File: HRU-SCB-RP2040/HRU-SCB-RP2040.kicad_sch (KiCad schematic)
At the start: 7 parts, among them J26 Pico_Socket_A, J27 Pico_Socket_B

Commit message: update: circuit design of HRU-SCB-RP2040
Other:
- moved on the sheet: A1
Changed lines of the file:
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@@
 (kicad_sch
-	(version 20231120)
+	(version 20250114)
 	(generator "eeschema")
-	(generator_version "8.0")
+	(generator_version "9.0")
 	(paper "A4")
 	(junction
@@
 	(label "SERVO.SERIAL1.TX"
 		(at 132.08 40.64 0)
-		(fields_autoplaced yes)
 		(effects
 			(font
@@
 	(label "I2C0.SCL"
 		(at 215.9 27.94 0)
-		(fields_autoplaced yes)
 		(effects
 			(font
@@
 	(label "SERVO.SERIAL1.TX"
 		(at 33.02 63.5 0)
-		(fields_autoplaced yes)
 		(effects
 			(font
@@
 	(label "SERVO.SERIAL0.RX"
 		(at 132.08 27.94 0)
-		(fields_autoplaced yes)
 		(effects
 			(font
@@
 	(label "SERVO.SERIAL1.DE"
 		(at 33.02 50.8 0)
-		(fields_autoplaced yes)
 		(effects
 			(font
@@
 	(label "SERVO.SERIAL1.DE"
 		(at 132.08 43.18 0)
-		(fields_autoplaced yes)
 		(effects
 			(font
@@
 	(label "SERVO.SERIAL0.DE"
 		(at 132.08 33.02 0)
-		(fields_autoplaced yes)
 		(effects
 			(font
@@
 	(label "SERVO.SERIAL0.RX"
 		(at 33.02 45.72 0)
-		(fields_autoplaced yes)
 		(effects
 			(font
@@
 	(label "SERVO.SERIAL1.RX"
 		(at 33.02 66.04 0)
-		(fields_autoplaced yes)
 		(effects
 			(font
@@
 	(label "I2C0.SDA"
 		(at 215.9 30.48 0)
-		(fields_autoplaced yes)
 		(effects
 			(font
@@
 	(label "SERVO.SERIAL1.RX"
 		(at 132.08 38.1 0)
-		(fields_autoplaced yes)
 		(effects
 			(font
@@
 	(label "SERVO.SERIAL0.TX"
 		(at 132.08 30.48 0)
-		(fields_autoplaced yes)
 		(effects
 			(font
@@
 	(label "SERVO.SERIAL0.DE"
 		(at 33.02 48.26 0)
-		(fields_autoplaced yes)
 		(effects
 			(font
@@
 	(label "I2C0.SDA"
 		(at 33.02 53.34 0)
-		(fields_autoplaced yes)
 		(effects
 			(font
@@
 	(label "SERVO.SERIAL0.TX"
 		(at 33.02 43.18 0)
-		(fields_autoplaced yes)
 		(effects
 			(font
@@
 	(label "I2C0.SCL"
 		(at 33.02 55.88 0)
-		(fields_autoplaced yes)
 		(effects
 			(font
@@
 	(symbol
 		(lib_id "MCU_Module_RaspberryPi_Pico:RaspberryPi_Pico_W_MultiPart-Module")
-		(at 76.2 66.04 90)
+		(at 76.2 66.04 0)
 		(unit 1)
 		(exclude_from_sim no)
@@
 		(fields_autoplaced yes)
 		(property "Reference" "A1"
-			(at 35.56 58.42 0)
+			(at 83.82 25.4 0)
 			(do_not_autoplace yes)
 			(effects
@@
 		)
 		(property "Value" "RaspberryPi_Pico_W"
-			(at 38.1 58.42 0)
+			(at 83.82 27.94 0)
 			(do_not_autoplace yes)
 			(effects
@@
 		)
 		(property "Footprint" "Module_RaspberryPi_Pico:RaspberryPi_Pico_W_Virtual"
-			(at 125.73 66.04 0)
+			(at 76.2 115.57 0)
 			(effects
 				(font
@@
 		)
 		(property "Datasheet" "https://datasheets.raspberrypi.com/picow/pico-w-datasheet.pdf"
-			(at 128.27 66.04 0)
+			(at 76.2 118.11 0)
 			(effects
 				(font
@@
 		)
 		(property "Description" "Versatile and inexpensive wireless microcontroller module (virtual representation) powered by RP2040 dual-core Arm Cortex-M0+ processor up to 133 MHz, 264kB SRAM, 2MB QSPI flash, Infineon CYW43439 2.4GHz 802.11n wireless LAN"
-			(at 130.81 66.04 0)
+			(at 76.2 120.65 0)
 			(effects
 				(font
@@
 		(at 152.4 25.4)
 		(size 38.1 20.32)
+		(exclude_from_sim no)
+		(in_bom yes)
+		(on_board yes)
+		(dnp no)
 		(fields_autoplaced yes)
 		(stroke
@@
 		(at 152.4 63.5)
 		(size 38.1 25.4)
+		(exclude_from_sim no)
+		(in_bom yes)
+		(on_board yes)
+		(dnp no)
 		(fields_autoplaced yes)
 		(stroke
@@
 		(at 228.6 25.4)
 		(size 38.1 38.1)
+		(exclude_from_sim no)
+		(in_bom yes)
+		(on_board yes)
+		(dnp no)
 		(fields_autoplaced yes)
 		(stroke
@@
 		)
 	)
+	(embedded_fonts no)
 )

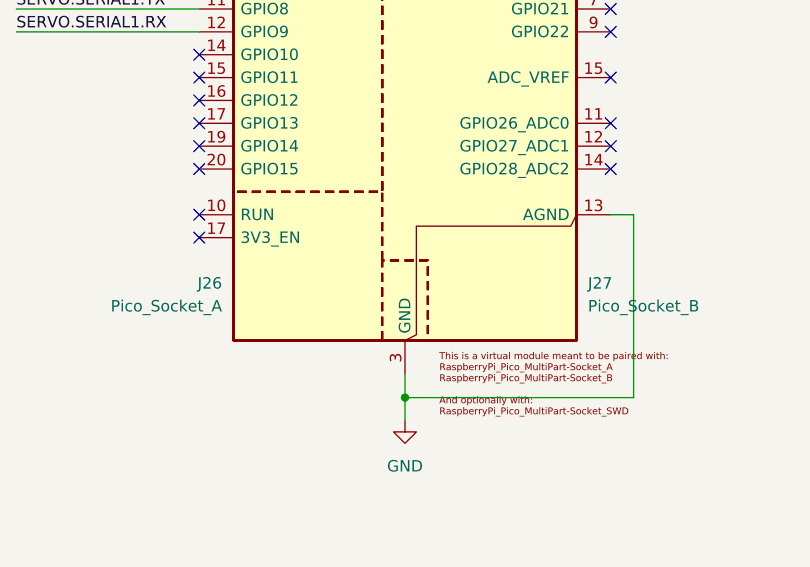
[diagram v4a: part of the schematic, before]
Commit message: Update: apply super DCDC
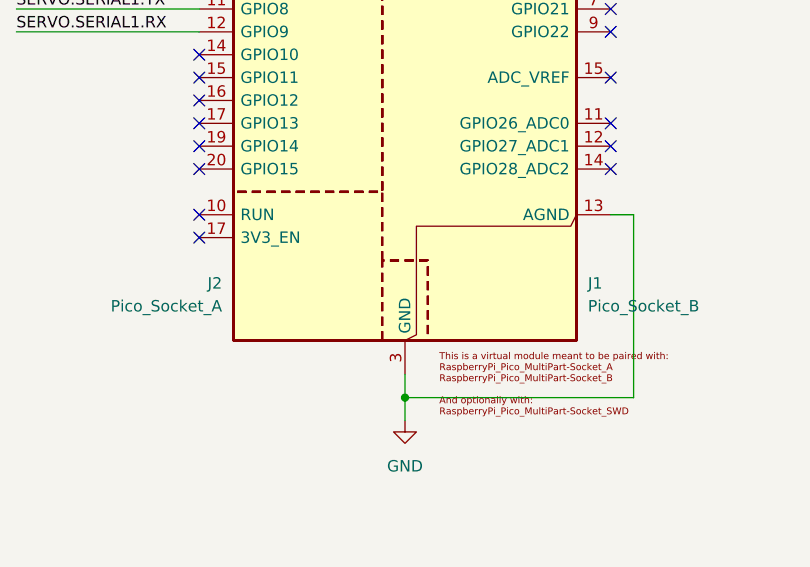
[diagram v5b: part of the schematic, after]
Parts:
- renumbered J27 to J1, J26 to J2
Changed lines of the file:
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@@
+			)
+		)
+		(property "AKI_CODE" ""
+			(at 215.9 101.6 0)
+			(effects
+				(font
+					(size 1.27 1.27)
+				)
+				(hide yes)
+			)
+		)
+		(property "AKI_URL" ""
+			(at 215.9 101.6 0)
+			(effects
+				(font
+					(size 1.27 1.27)
+				)
+				(hide yes)
 			)
 		)
@@
 			)
 		)
+		(property "AKI_CODE" ""
+			(at 76.2 66.04 0)
+			(effects
+				(font
+					(size 1.27 1.27)
+				)
+				(hide yes)
+			)
+		)
+		(property "AKI_URL" ""
+			(at 76.2 66.04 0)
+			(effects
+				(font
+					(size 1.27 1.27)
+				)
+				(hide yes)
+			)
+		)
 		(instances
 			(project ""
@@
 			)
 		)
+		(property "AKI_CODE" ""
+			(at 215.9 124.46 0)
+			(effects
+				(font
+					(size 1.27 1.27)
+				)
+				(hide yes)
+			)
+		)
+		(property "AKI_URL" ""
+			(at 215.9 124.46 0)
+			(effects
+				(font
+					(size 1.27 1.27)
+				)
+				(hide yes)
+			)
+		)
 		(instances
 			(project "HRU-SCB-RP2040"
@@
 			)
 		)
+		(property "AKI_CODE" ""
+			(at 215.9 116.84 0)
+			(effects
+				(font
+					(size 1.27 1.27)
+				)
+				(hide yes)
+			)
+		)
+		(property "AKI_URL" ""
+			(at 215.9 116.84 0)
+			(effects
+				(font
+					(size 1.27 1.27)
+				)
+				(hide yes)
+			)
+		)
 		(instances
 			(project "HRU-SCB-RP2040"
@@
 		(dnp no)
 		(fields_autoplaced yes)
-		(property "Reference" "J27"
+		(property "Reference" "J1"
 			(at 96.52 93.98 0)
 			(do_not_autoplace yes)
@@
 			)
 		)
+		(property "AKI_CODE" ""
+			(at 76.2 66.04 0)
+			(effects
+				(font
+					(size 1.27 1.27)
+				)
+				(hide yes)
+			)
+		)
+		(property "AKI_URL" ""
+			(at 76.2 66.04 0)
+			(effects
+				(font
+					(size 1.27 1.27)
+				)
+				(hide yes)
+			)
+		)
 		(pin "13"
 		)
@@
 			(project ""
 				(path "/22d57d1f-fa00-4148-a62a-8eb596ebbd21"
-					(reference "J27")
+					(reference "J1")
 					(unit 1)
 				)
@@
 			)
 		)
+		(property "AKI_CODE" ""
+			(at 215.9 109.22 0)
+			(effects
+				(font
+					(size 1.27 1.27)
+				)
+				(hide yes)
+			)
+		)
+		(property "AKI_URL" ""
+			(at 215.9 109.22 0)
+			(effects
+				(font
+					(size 1.27 1.27)
+				)
+				(hide yes)
+			)
+		)
 		(instances
 			(project "HRU-SCB-RP2040"
@@
 		(dnp no)
 		(fields_autoplaced yes)
-		(property "Reference" "J26"
+		(property "Reference" "J2"
 			(at 55.88 93.98 0)
 			(do_not_autoplace yes)
@@
 			)
 		)
+		(property "AKI_CODE" ""
+			(at 76.2 66.04 0)
+			(effects
+				(font
+					(size 1.27 1.27)
+				)
+				(hide yes)
+			)
+		)
+		(property "AKI_URL" ""
+			(at 76.2 66.04 0)
+			(effects
+				(font
+					(size 1.27 1.27)
+				)
+				(hide yes)
+			)
+		)
 		(pin "15"
 		)
@@
 			(project ""
 				(path "/22d57d1f-fa00-4148-a62a-8eb596ebbd21"
-					(reference "J26")
-					(unit 1)
-				)
+					(reference "J2")
+					(unit 1)
+				)

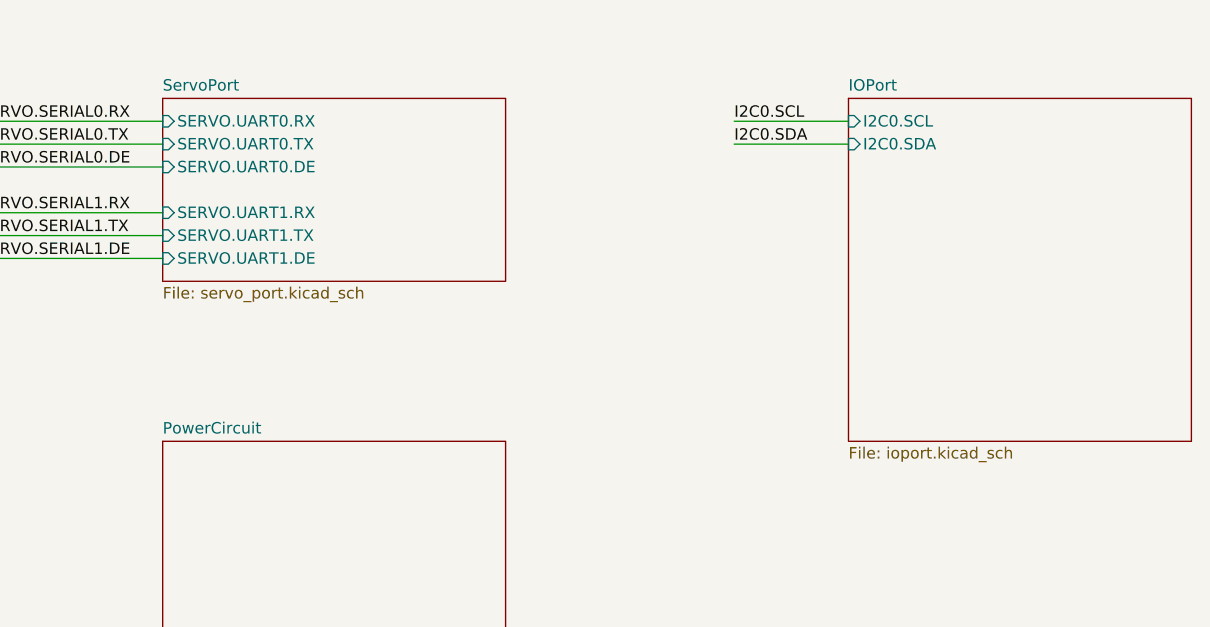
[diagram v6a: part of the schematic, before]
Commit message: fix(HRU-SCB-RP2040): assign 3V3 to I2C's VCC and refactor parts layout
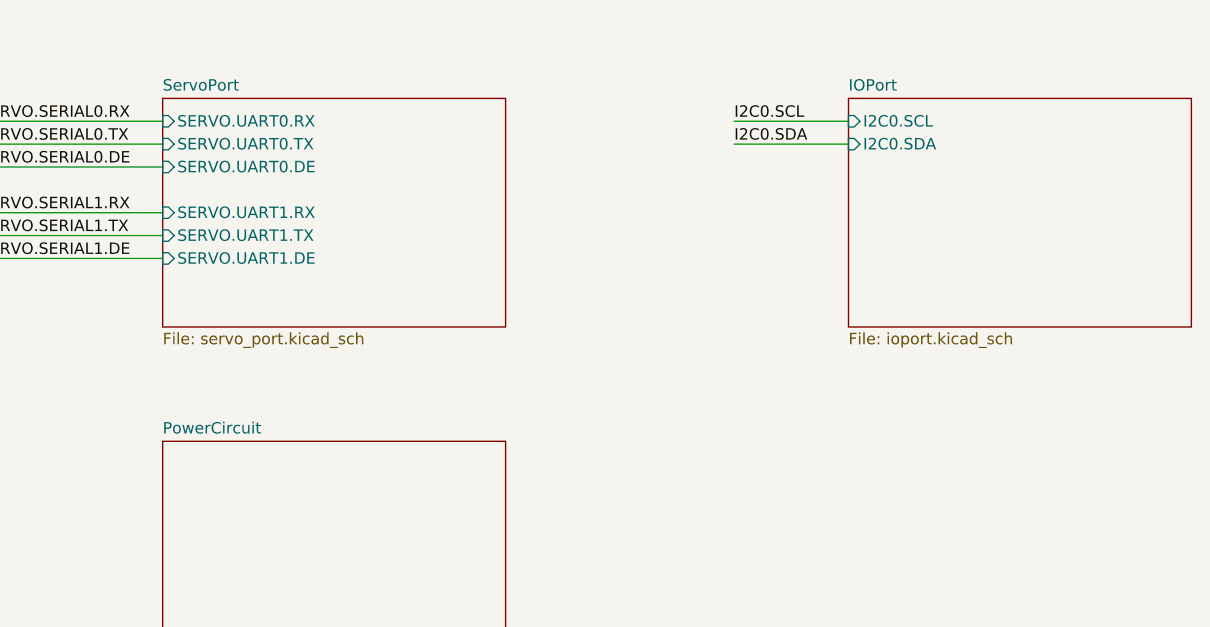
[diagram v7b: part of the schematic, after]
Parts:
- J1, J2: AKI_CODE (none) -> 103077; AKI_URL (none) -> https://akizukidenshi.com/catalog/g/g103077/
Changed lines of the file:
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@@
 			)
 		)
-		(property "AKI_CODE" ""
+		(property "AKI_CODE" "103077"
 			(at 76.2 66.04 0)
 			(hide yes)
@@
 			)
 		)
-		(property "AKI_URL" ""
+		(property "AKI_URL" "https://akizukidenshi.com/catalog/g/g103077/"
 			(at 76.2 66.04 0)
 			(hide yes)
@@
 			)
 		)
-		(property "AKI_CODE" ""
+		(property "AKI_CODE" "103077"
 			(at 76.2 66.04 0)
 			(hide yes)
@@
 			)
 		)
-		(property "AKI_URL" ""
+		(property "AKI_URL" "https://akizukidenshi.com/catalog/g/g103077/"
 			(at 76.2 66.04 0)
 			(hide yes)
@@
 	(sheet
 		(at 152.4 25.4)
-		(size 38.1 20.32)
+		(size 38.1 25.4)
 		(exclude_from_sim no)
 		(in_bom yes)
@@
 		)
 		(property "Sheetfile" "servo_port.kicad_sch"
-			(at 152.4 46.3046 0)
+			(at 152.4 51.3846 0)
 			(show_name no)
 			(do_not_autoplace no)
@@
 	(sheet
 		(at 228.6 25.4)
-		(size 38.1 38.1)
+		(size 38.1 25.4)
 		(exclude_from_sim no)
 		(in_bom yes)
@@
 		)
 		(property "Sheetfile" "ioport.kicad_sch"
-			(at 228.6 64.0846 0)
-			(show_name no)
-			(do_not_autoplace no)
+			(at 228.6 51.3846 0)
+			(show_name no)
+			(do_not_autoplace no)
